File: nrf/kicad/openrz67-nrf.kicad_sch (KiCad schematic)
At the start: 15 parts, among them J1 Camera, J2 SWD, Q1 AO3401A, SW1 B3U-1000P, U1 E73-2G4M08S1F, U2 TLP172AM, U3 TLP172AM

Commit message: nrf: readable schematic layout
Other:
- note added: "Button, status LED"
- note added: "Debug"
- note added: "MCU"
- note added: "Power, reverse-cell block"
- note added: "Shutter: PhotoMOS relays, camera port"

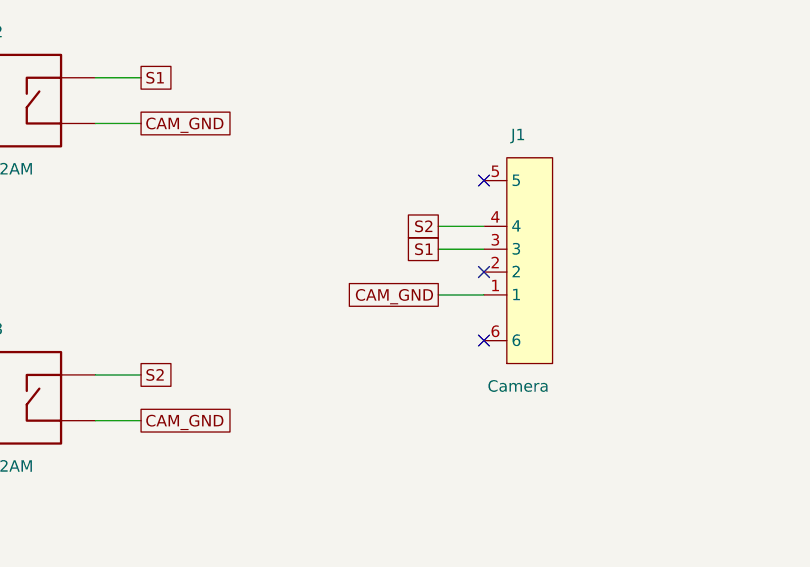
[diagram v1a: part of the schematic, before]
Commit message: nrf: camera connector in camera pin order (rev B)
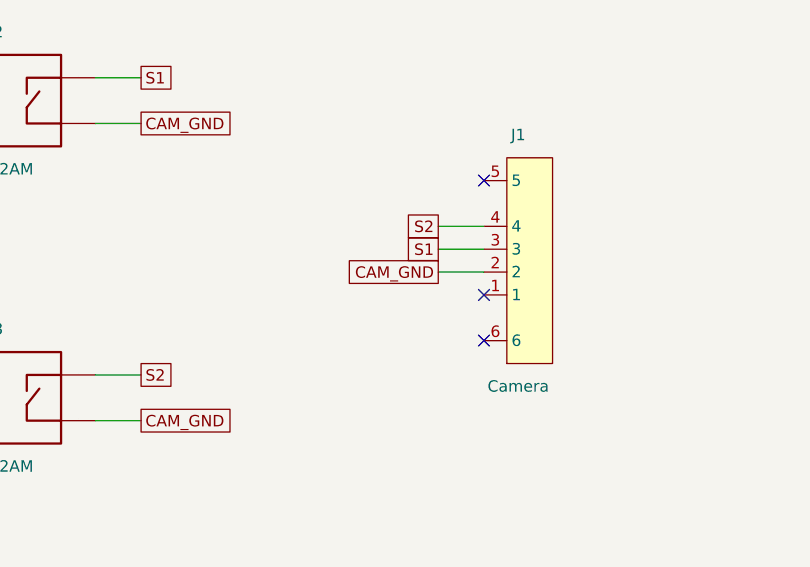
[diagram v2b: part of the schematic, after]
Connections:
- net CAM_GND: now also J1.2; no longer J1.1
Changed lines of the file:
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@@
   (wire (pts (xy 39.37 33.02) (xy 34.29 33.02)) (stroke (width 0) (type default)))
   (wire (pts (xy 39.37 35.56) (xy 34.29 35.56)) (stroke (width 0) (type default)))
-  (wire (pts (xy 245.11 110.49) (xy 240.03 110.49)) (stroke (width 0) (type default)))
+  (wire (pts (xy 245.11 107.95) (xy 240.03 107.95)) (stroke (width 0) (type default)))
   (wire (pts (xy 245.11 105.41) (xy 240.03 105.41)) (stroke (width 0) (type default)))
   (wire (pts (xy 245.11 102.87) (xy 240.03 102.87)) (stroke (width 0) (type default)))
@@
     (effects (font (size 1.27 1.27)) (justify right))
   )
-  (global_label "CAM_GND" (shape passive) (at 240.03 110.49 180) (fields_autoplaced yes)
+  (global_label "CAM_GND" (shape passive) (at 240.03 107.95 180) (fields_autoplaced yes)
     (effects (font (size 1.27 1.27)) (justify right))
   )
@@
   (no_connect (at 80.01 97.79))
   (no_connect (at 80.01 95.25))
-  (no_connect (at 245.11 107.95))
+  (no_connect (at 245.11 110.49))
   (no_connect (at 245.11 97.79))
   (no_connect (at 245.11 115.57))
